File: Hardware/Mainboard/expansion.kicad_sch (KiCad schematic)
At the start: 0 parts

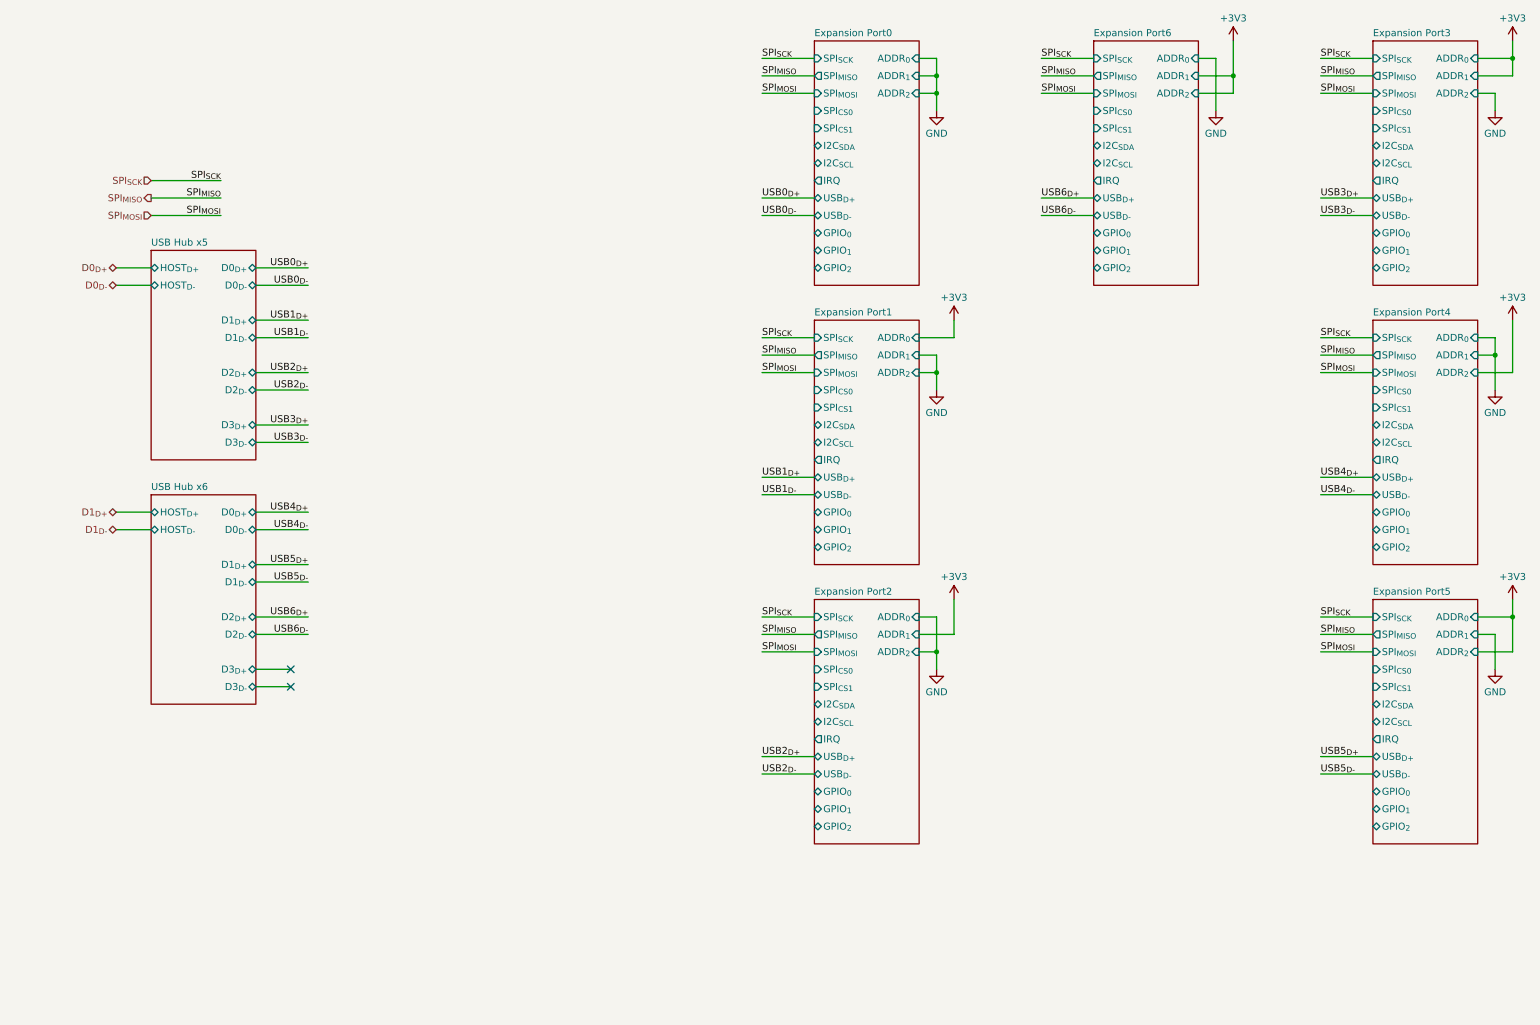
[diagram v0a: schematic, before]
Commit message: Adds more work on the mainboard schematic
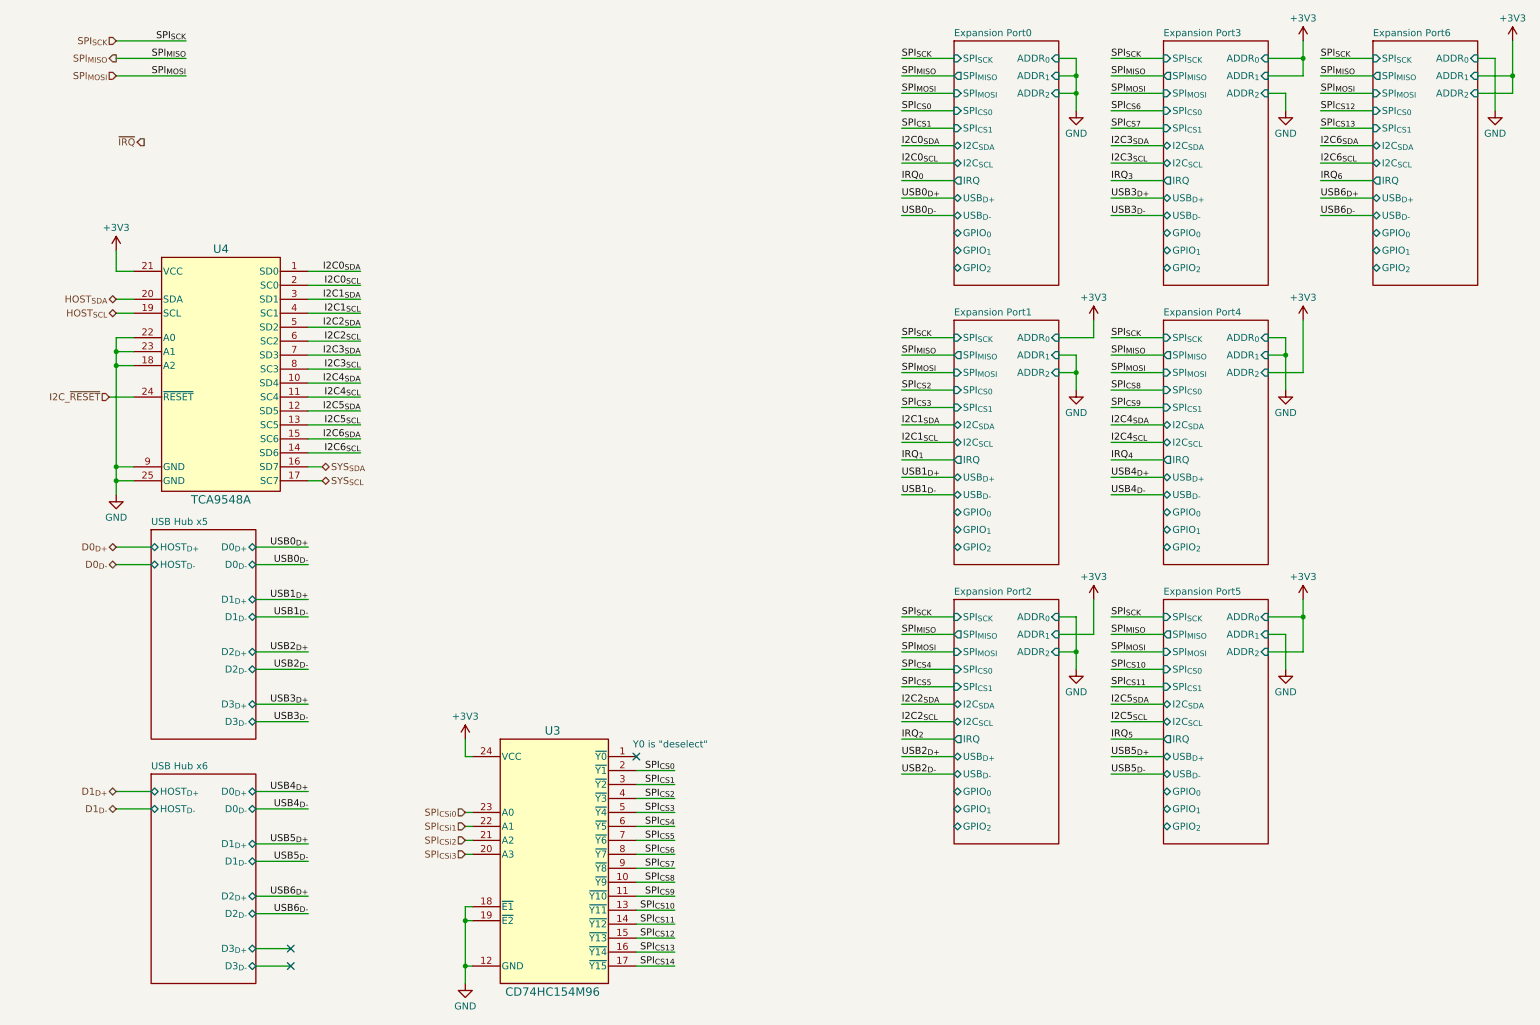
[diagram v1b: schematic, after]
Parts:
- added U3: CD74HC154M96, compi:CD74HC154M96, symbol compi:CD74HC154M96
- added U4: TCA9548A, compi:TCA9548ARGERQ1, symbol compi:TCA9548ARGERQ1
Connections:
- net +3V3: now also U3.24 (VCC), U4.21 (VCC)
- net GND: now also U3.12 (GND), U3.18 (~{E1}), U3.19 (~{E2}), U4.18 (A2), U4.22 (A0), U4.23 (A1), U4.25 (GND), U4.9 (GND)
- new net HOST_{SCL}: U4.19 (SCL)
- new net HOST_{SDA}: U4.20 (SDA)
- new net I2C0_{SCL}: U4.2 (SC0)
- new net I2C0_{SDA}: U4.1 (SD0)
- new net I2C1_{SCL}: U4.4 (SC1)
- new net I2C1_{SDA}: U4.3 (SD1)
- new net I2C2_{SCL}: U4.6 (SC2)
- new net I2C2_{SDA}: U4.5 (SD2)
- new net I2C3_{SCL}: U4.8 (SC3)
- new net I2C3_{SDA}: U4.7 (SD3)
- new net I2C4_{SCL}: U4.11 (SC4)
- new net I2C4_{SDA}: U4.10 (SD4)
- new net I2C5_{SCL}: U4.13 (SC5)
- new net I2C5_{SDA}: U4.12 (SD5)
- new net I2C6_{SCL}: U4.14 (SD6)
- new net I2C6_{SDA}: U4.15 (SC6)
- new net I2C_~{RESET}: U4.24 (~{RESET})
- new net SPI_{CS0}: U3.2 (~{Y1})
- new net SPI_{CS10}: U3.13 (~{Y11})
- new net SPI_{CS11}: U3.14 (~{Y12})
- new net SPI_{CS12}: U3.15 (~{Y13})
- new net SPI_{CS13}: U3.16 (~{Y14})
- new net SPI_{CS14}: U3.17 (~{Y15})
- new net SPI_{CS1}: U3.3 (~{Y2})
- new net SPI_{CS2}: U3.4 (~{Y3})
- new net SPI_{CS3}: U3.5 (~{Y4})
- new net SPI_{CS4}: U3.6 (~{Y5})
- new net SPI_{CS5}: U3.7 (~{Y6})
- new net SPI_{CS6}: U3.8 (~{Y7})
- new net SPI_{CS7}: U3.9 (~{Y8})
- new net SPI_{CS8}: U3.10 (~{Y9})
- new net SPI_{CS9}: U3.11 (~{Y10})
- new net SPI_{CSi0}: U3.23 (A0)
- new net SPI_{CSi1}: U3.22 (A1)
- new net SPI_{CSi2}: U3.21 (A2)
- new net SPI_{CSi3}: U3.20 (A3)
- new net SYS_{SCL}: U4.17 (SC7)
- new net SYS_{SDA}: U4.16 (SD7)
- no-connect marks 2 -> 3
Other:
- note added: "Y0 is "deselect""

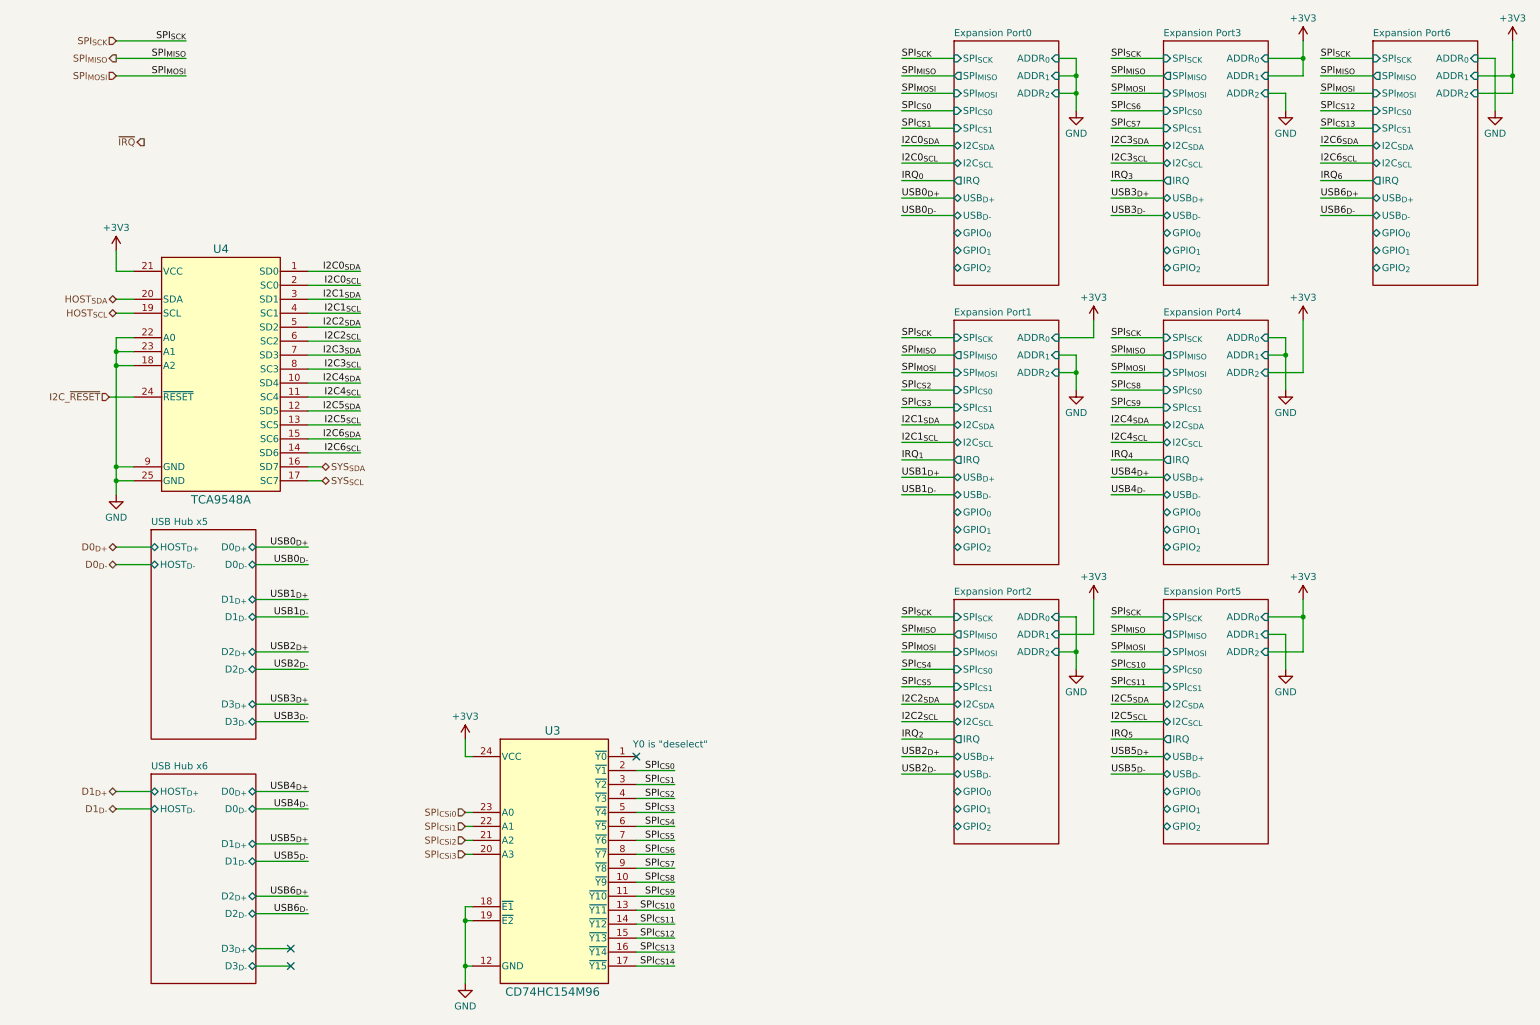
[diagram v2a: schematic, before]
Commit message: Adds pull-ups and irq controller to expansion subsystem
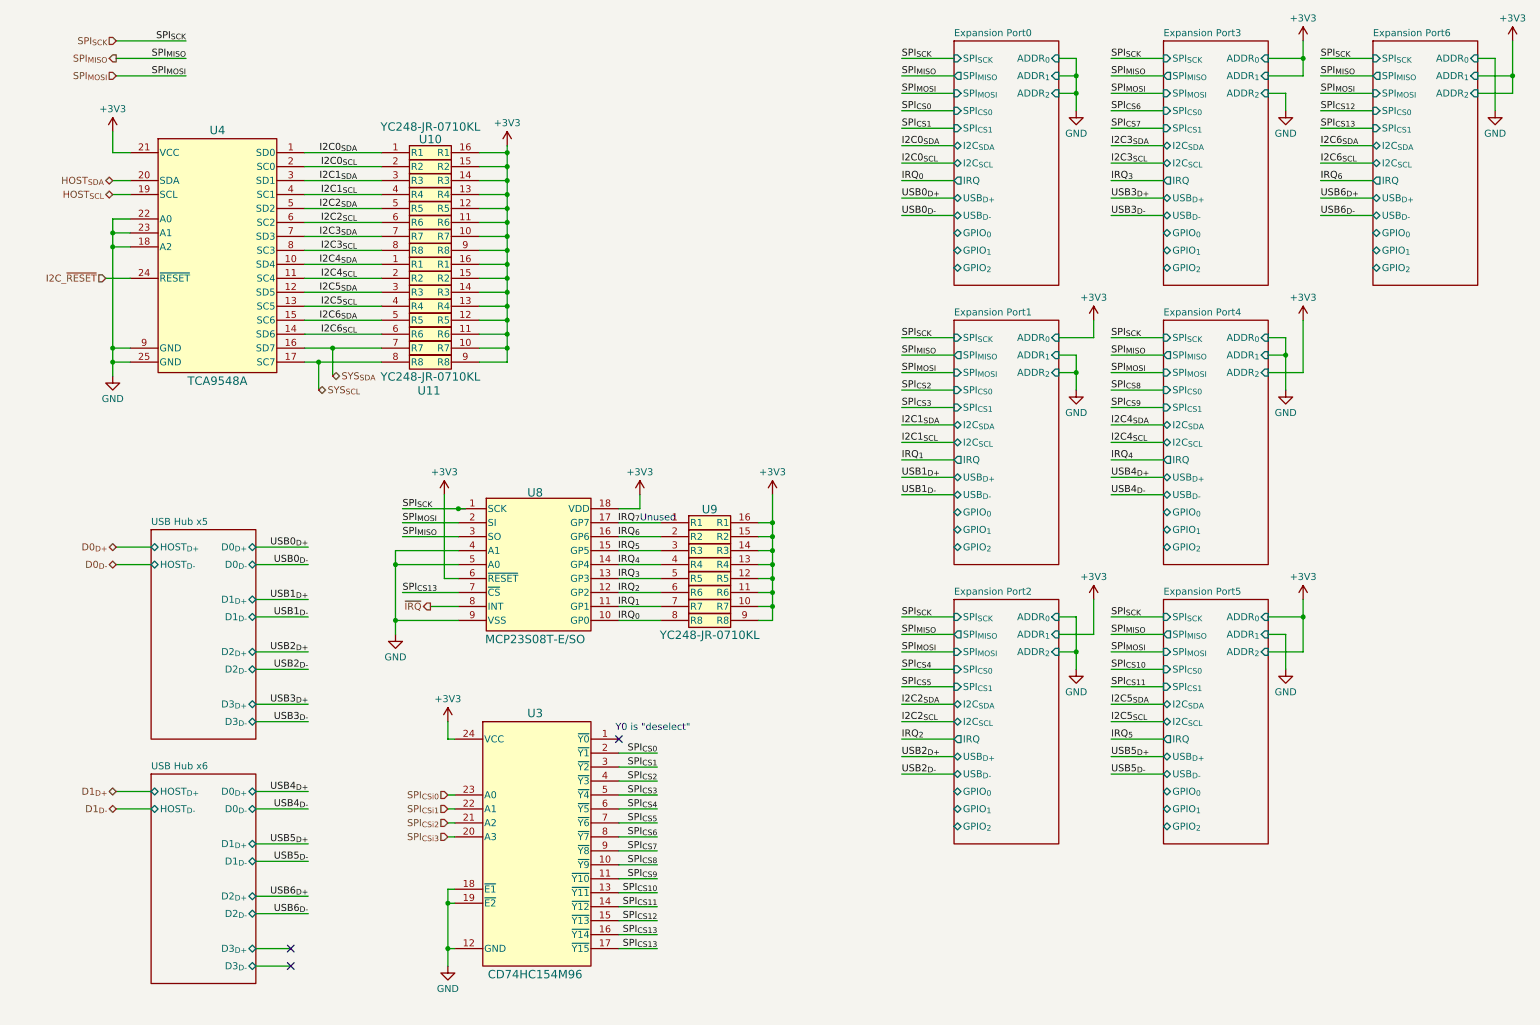
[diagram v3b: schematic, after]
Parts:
- added U10, U11, U9: YC248-JR-0710KL, compi:YC248-JR-0710KL, symbol compi:YC248-JR-0710KL
- added U8: MCP23S08T-E/SO, compi:MCP23S08T-E_SO, symbol compi:MCP23S08T-E/SO
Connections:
- net SPI_{CS14} is gone; now on net SPI_{CS13}: U3.17 (~{Y15})
- net +3V3: now also U10.10 (R7), U10.11 (R6), U10.12 (R5), U10.13 (R4), U10.14 (R3), U10.15 (R2), U10.16 (R1), U10.9 (R8), U11.10 (R7), U11.11 (R6), U11.12 (R5), U11.13 (R4), U11.14 (R3), U11.15 (R2), U11.16 (R1), U11.9 (R8), U8.18 (VDD), U8.6 (~{RESET}), U9.10 (R7), U9.11 (R6), U9.12 (R5), U9.13 (R4), U9.14 (R3), U9.15 (R2), U9.16 (R1), U9.9 (R8)
- net GND: now also U8.4 (A1), U8.5 (A0), U8.9 (VSS)
- net I2C0_{SCL}: now also U10.2 (R2)
- net I2C0_{SDA}: now also U10.1 (R1)
- net I2C1_{SCL}: now also U10.4 (R4)
- net I2C1_{SDA}: now also U10.3 (R3)
- net I2C2_{SCL}: now also U10.6 (R6)
- net I2C2_{SDA}: now also U10.5 (R5)
- net I2C3_{SCL}: now also U10.8 (R8)
- net I2C3_{SDA}: now also U10.7 (R7)
- net I2C4_{SCL}: now also U11.2 (R2)
- net I2C4_{SDA}: now also U11.1 (R1)
- net I2C5_{SCL}: now also U11.4 (R4)
- net I2C5_{SDA}: now also U11.3 (R3)
- net I2C6_{SCL}: now also U11.6 (R6)
- net I2C6_{SDA}: now also U11.5 (R5)
- net IRQ_{0}: now also U8.10 (GP0), U9.8 (R8)
- net IRQ_{1}: now also U8.11 (GP1), U9.7 (R7)
- net IRQ_{2}: now also U8.12 (GP2), U9.6 (R6)
- net IRQ_{3}: now also U8.13 (GP3), U9.5 (R5)
- net IRQ_{4}: now also U8.14 (GP4), U9.4 (R4)
- net IRQ_{5}: now also U8.15 (GP5), U9.3 (R3)
- net IRQ_{6}: now also U8.16 (GP6), U9.2 (R2)
- net SPI_{CS13}: now also U8.7 (~{CS})
- net SPI_{MISO}: now also U8.3 (SO)
- net SPI_{MOSI}: now also U8.2 (SI)
- net SPI_{SCK}: now also U8.1 (SCK)
- net SYS_{SCL}: now also U11.8 (R8)
- net SYS_{SDA}: now also U11.7 (R7)
- net ~{IRQ}: now also U8.8 (INT)
- new net IRQ_{7}: U8.17 (GP7), U9.1 (R1)
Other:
- note added: "Unused"
- moved on the sheet: U3, U4
